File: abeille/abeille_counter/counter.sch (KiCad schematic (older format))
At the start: 3 parts, among them IC1 ATMEGA328-P

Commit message: abeille counter schematics update
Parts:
- removed D1: LED, LEDs:LED-3MM, symbol LED
- removed IC1: ATMEGA328-P, Housings_DIP:DIP-28_W7.62mm_LongPads, symbol ATMEGA328-P
- added P1, P2: HE10-10, symbol HE10-10
- added R10, R11, R12, R21, R22, R23, R24, R33, R34, R35, R36, R45, R46, R47, R48, R9: 100K, Resistors_ThroughHole:Resistor_Horizontal_RM10mm, symbol R
- added R13, R14, R15, R16, R17, R18, R19, R2, R20, R25, R26, R27, R28, R29, R3, R30, R31, R32, R37, R38, R39, R4, R40, R41, R42, R43, R44, R5, R6, R7, R8: 1K, Resistors_ThroughHole:Resistor_Horizontal_RM10mm, symbol R
- added R49, R50, R51, R52, R53, R54, R55, R56, R57: 0, Resistors_ThroughHole:Resistor_Horizontal_RM10mm, symbol R
- added U1: IN_0, DIP-4, symbol ITR-9608
- added U10: OUT_2, DIP-4, symbol ITR-9608
- added U11: IN_6, DIP-4, symbol ITR-9608
- added U12: OUT_6, DIP-4, symbol ITR-9608
- added U13: IN_3, DIP-4, symbol ITR-9608
- added U14: OUT_3, DIP-4, symbol ITR-9608
- added U15: IN_7, DIP-4, symbol ITR-9608
- added U16: OUT_7, DIP-4, symbol ITR-9608
- added U17: pca9555, symbol pca9555
- added U2: OUT_0, DIP-4, symbol ITR-9608
- added U3: IN_4, DIP-4, symbol ITR-9608
- added U4: OUT_4, DIP-4, symbol ITR-9608
- added U5: IN_1, DIP-4, symbol ITR-9608
- added U6: OUT_1, DIP-4, symbol ITR-9608
- added U7: IN_5, DIP-4, symbol ITR-9608
- added U8: OUT_5, DIP-4, symbol ITR-9608
- added U9: IN_2, DIP-4, symbol ITR-9608
- R1: value 1000 -> 1K
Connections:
- net +5V: now also R1.1, R10.1, R11.1, R12.1, R13.1, R14.1, R15.1, R16.1, R2.1, R21.1, R22.1, R23.1, R24.1, R25.1, R26.1, R27.1, R28.1, R3.1, R33.1, R34.1, R35.1, R36.1, R37.1, R38.1, R39.1, R4.1, R40.1, R45.1, R46.1, R47.1, R48.1, R9.1
- net GND: now also P1.1, P1.2, P2.1, P2.2, R17.2, R18.2, R19.2, R20.2, R29.2, R30.2, R31.2, R32.2, R41.2, R42.2, R43.2, R44.2, R5.2, R6.2, R7.2, R8.2, U1.2, U10.2, U11.2, U12.2, U13.2, U14.2, U15.2, U16.2, U17.12 (VSS), U2.2, U3.2, U4.2, U5.2, U6.2, U7.2, U8.2, U9.2
- net at R1.2: now also U1.1
- new net: R9.2, U1.3
- new net: R5.1, U1.4
- new net: R2.2, U2.1
- new net: R6.1, U2.4
- new net: R13.2, U5.1
- new net: R21.2, U5.3
- new net: R17.1, U5.4
- new net: R14.2, U6.1
- new net: R18.1, U6.4
- new net: R25.2, U9.1
- new net: R33.2, U9.3
- new net: R29.1, U9.4
- new net: R26.2, U10.1
- new net: R30.1, U10.4
- new net: R37.2, U13.1
- new net: R45.2, U13.3
- new net: R41.1, U13.4
- new net: R38.2, U14.1
- new net: R42.1, U14.4
- new net: R3.2, U3.1
- new net: R10.2, U3.3
- new net: R7.1, U3.4
- new net: R4.2, U4.1
- new net: R8.1, U4.4
- new net: R15.2, U7.1
- new net: R22.2, U7.3
- new net: R19.1, U7.4
- new net: R16.2, U8.1
- new net: R20.1, U8.4
- new net: R27.2, U11.1
- new net: R34.2, U11.3
- new net: R31.1, U11.4
- new net: R28.2, U12.1
- new net: R32.1, U12.4
- new net: R39.2, U15.1
- new net: R46.2, U15.3
- new net: R43.1, U15.4
- new net: R40.2, U16.1
- new net: R44.1, U16.4
- new net: P1.4, R49.2
- new net: P1.6, R50.2
- new net: P1.8, R51.2
- new net 5V: P1.10, P1.9, P2.10, P2.9, U17.24 (VDD)
- new net A0: P2.6, R49.1, R52.2, R53.1, U17.21 (A0)
- new net A1: P2.8, R50.1, R54.2, R55.1, U17.2 (A1)
- new net A2: P2.4, R51.1, R56.2, R57.1, U17.3 (A2)
- new net D0: U17.4 (IO0_0)
- new net D1: R11.2, U17.5 (IO0_1), U2.3
- new net D10: U17.15 (IO1_2)
- new net D11: R24.2, U17.16 (IO1_3), U8.3
- new net D12: U17.17 (IO1_4)
- new net D13: R36.2, U12.3, U17.18 (IO1_5)
- new net D14: U17.19 (IO1_6)
- new net D15: R48.2, U16.3, U17.20 (IO1_7)
- new net D2: U17.6 (IO0_2)
- new net D3: R23.2, U17.7 (IO0_3), U6.3
- new net D4: U17.8 (IO0_4)
- new net D5: R35.2, U10.3, U17.9 (IO0_5)
- new net D6: U17.10 (IO0_6)
- new net D7: R47.2, U14.3, U17.11 (IO0_7)
- new net D8: U17.13 (IO1_0)
- new net D9: R12.2, U17.14 (IO1_1), U4.3
- new net INT#: P1.7, P2.7, U17.1 (INT#)
- new net SCL: P1.3, P2.3, U17.22 (SCL)
- new net SDA: P1.5, P2.5, U17.23 (SDA)
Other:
- note added: "female"
- note added: "male"
- moved on the sheet: R1

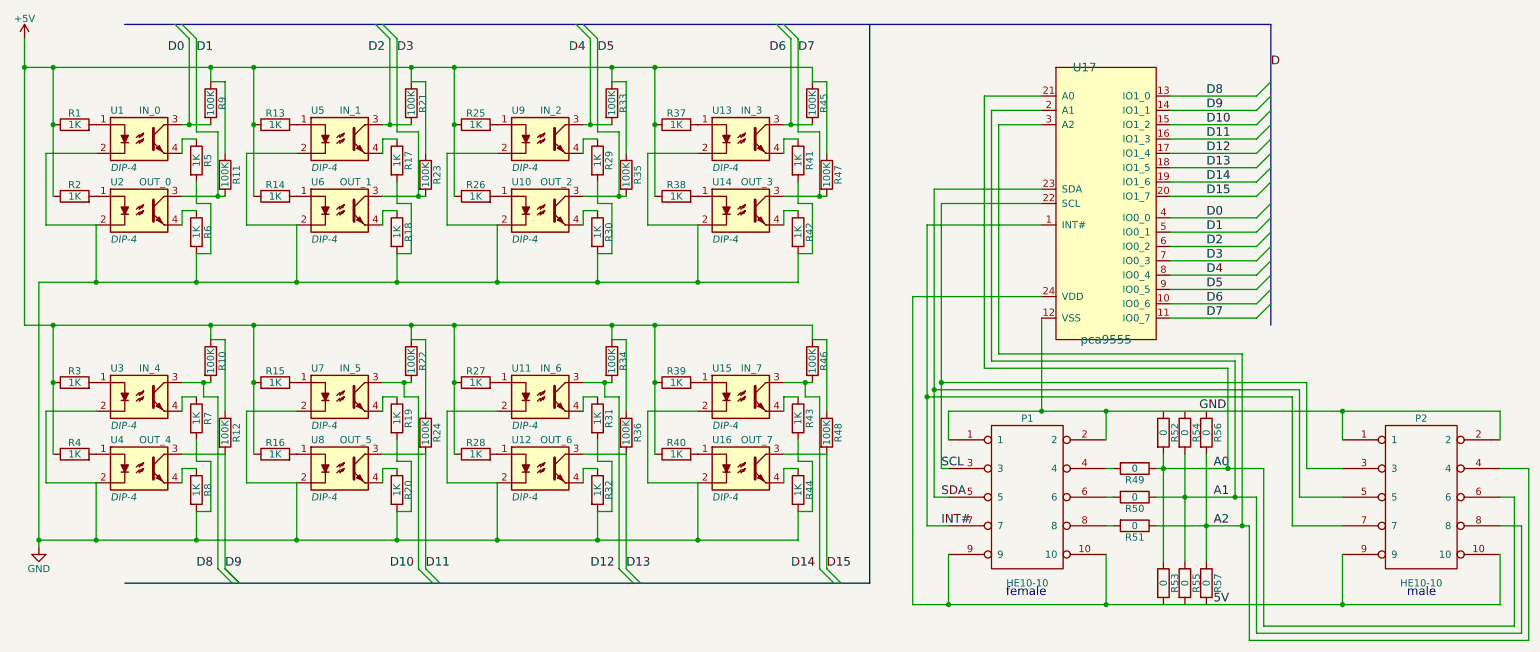
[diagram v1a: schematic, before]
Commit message: start placing counter components
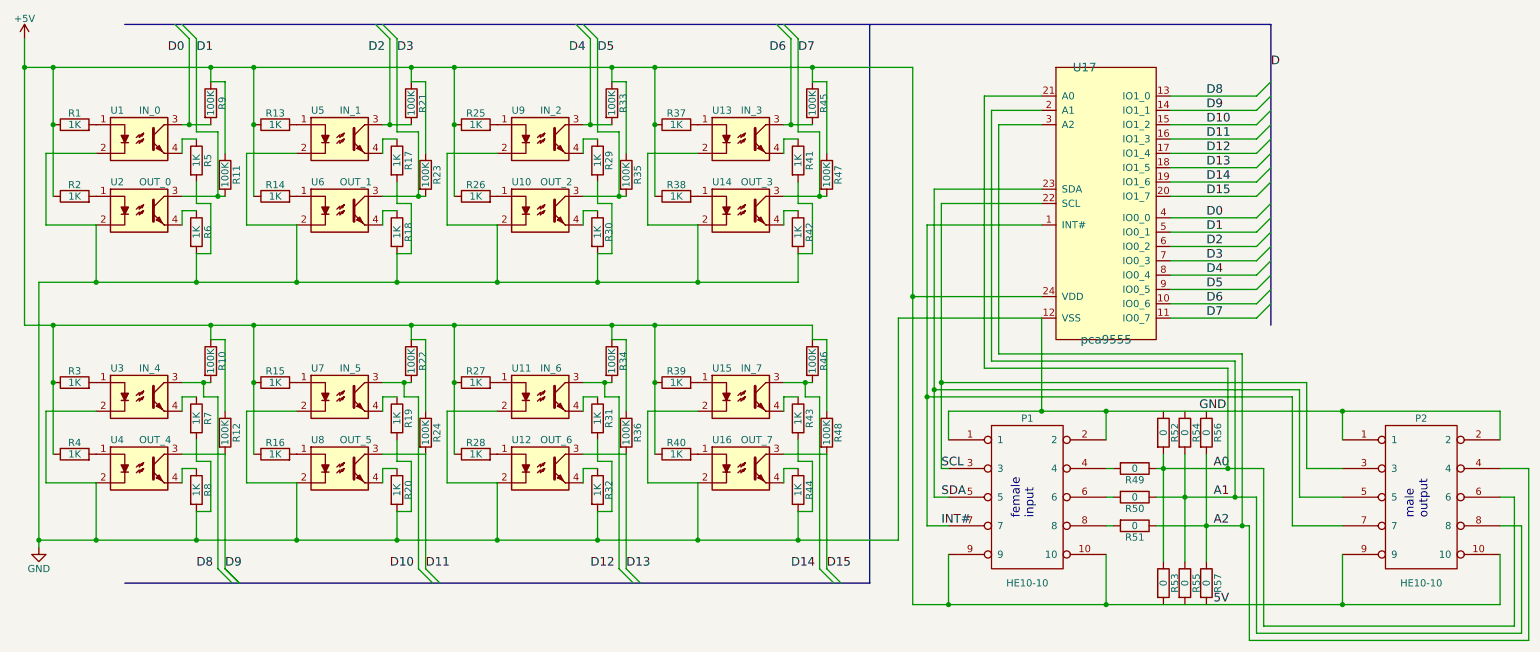
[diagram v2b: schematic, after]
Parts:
- P1, P2: footprint (none) -> Connect:IDC_Header_Straight_10pins
- R1, R10, R11, R12, R13, R14, R15, R16, R17, R18, R19, R2, R20, R21, R22, R23, R24, R25, R26, R27, R28, R29, R3, R30, R31, R32, R33, R34, R35, R36, R37, R38, R39, R4, R40, R41, R42, R43, R44, R45, R46, R47, R48, R49, R5, R50, R51, R52, R53, R54, R55, R56, R57, R6, R7, R8, R9: footprint Resistors_ThroughHole:Resistor_Horizontal_RM10mm -> Resistors_SMD:R_1206_HandSoldering
- U1, U10, U11, U12, U13, U14, U15, U16, U2, U3, U4, U5, U6, U7, U8, U9: footprint DIP-4 -> counter_footprint:ITR9608_DIP-4_0_ELL
- U17: footprint (none) -> Housings_DIP:DIP-24_W15.24mm_LongPads
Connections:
- net 5V is gone; now on net +5V: P1.10, P1.9, P2.10, P2.9, U17.24 (VDD)
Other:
- note added: "female\ninput"
- note added: "male\noutput"
- note removed: "female"
- note removed: "male"

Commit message: start placing of resistor of abeille_counter
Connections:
- net +5V: now also R53.2, R55.2, R57.2
- net GND: now also R52.1, R54.1, R56.1
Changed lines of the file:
@@
 	6700 3850 7700 3850
 Connection ~ 6000 5400
+Connection ~ 8550 4500
+Connection ~ 8700 4500
+Connection ~ 8850 4500
+Connection ~ 8550 5850
+Connection ~ 8700 5850
+Connection ~ 8850 5850
 $EndSCHEMATC

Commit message: first final routing version of abeille counter
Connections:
- net D0: now also R9.2, U1.3
- net D10: now also R22.2, U7.3
- net D12: now also R34.2, U11.3
- net D14: now also R46.2, U15.3
- net D2: now also R21.2, U5.3
- net D4: now also R33.2, U9.3
- net D6: now also R45.2, U13.3
- net D8: now also R10.2, U3.3
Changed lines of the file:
@@
 Entry Wire Line
 	5900 1800 6000 1900
-Text Label 1600 2000 0    60   ~ 0
+Text Label 1750 2200 0    60   ~ 0
 D0
 Text Label 1800 2000 0    60   ~ 0
 D1
-Text Label 3000 2000 0    60   ~ 0
+Text Label 3150 2200 0    60   ~ 0
 D2
 Text Label 3200 2000 0    60   ~ 0
 D3
-Text Label 4400 2000 0    60   ~ 0
+Text Label 4550 2200 0    60   ~ 0
 D4
 Text Label 4600 2000 0    60   ~ 0
 D5
-Text Label 5800 2000 0    60   ~ 0
-D6
-Text Label 6000 2000 0    60   ~ 0
-D7
 Entry Wire Line
 	1950 5600 2050 5700
@@
 Entry Wire Line
 	6200 5600 6300 5700
-Text Label 1800 5600 0    60   ~ 0
+Text Label 1950 5500 0    60   ~ 0
 D8
 Entry Wire Line
@@
 Text Label 2000 5600 0    60   ~ 0
 D9
-Text Label 3150 5600 0    60   ~ 0
+Text Label 3350 5500 0    60   ~ 0
 D10
 Text Label 3400 5600 0    60   ~ 0
 D11
-Text Label 4550 5600 0    60   ~ 0
+Text Label 4750 5500 0    60   ~ 0
 D12
 Text Label 4800 5600 0    60   ~ 0
 D13
-Text Label 5950 5600 0    60   ~ 0
+Text Label 6150 5500 0    60   ~ 0
 D14
 Text Label 6200 5600 0    60   ~ 0
@@
 Connection ~ 8700 5850
 Connection ~ 8850 5850
+Text Label 6000 2000 0    60   ~ 0
+D7
+Text Label 5950 2200 0    60   ~ 0
+D6
 $EndSCHEMATC
